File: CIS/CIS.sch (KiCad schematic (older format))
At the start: 181 parts, among them P3 K_0023, U14 U_0101, U16 U_0049, U17 U_0049, U2 STM32H745IIKx

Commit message: Schematic part finished
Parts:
- removed C?: C_0003, DVB_Capacitors_Ceramic:C_0603, symbol CIS-rescue:C_0003-HM3-rescue
- removed C?: C_0007, DVB_Capacitors_Ceramic:C_1206, symbol DVB_C:C_0007
- removed C?: C_0002, DVB_Capacitors_Ceramic:C_0402, symbol CIS-rescue:C_0002-HM3-rescue
- removed F?: F_0002, DVB_F:F_1206, symbol DVB_F:F_0002
- removed K?: K_0042, DVB_Connectors:USB_Mini-B_Lumberg_2486_01_Horizontal, symbol DVB_K:K_0042
- removed L?: L_0009, DVB_Inductors:L_4018-Coilcraft, symbol DVB_L:L_0009
- removed R?: R_0117, DVB_Resistors:R_0402, symbol DVB_R:R_0117
- removed R?: R_0064, DVB_Resistors:R_0402, symbol DVB_R:R_0064
- removed U?: U_0063, DVB_SSOP:MSOP_10-3x3_P0.5, symbol DVB_U:U_0063
- removed U?: U_0054, DVB_SOT:SOT_363-SC_70-6, symbol DVB_U:U_0054
- added C87, C?: C_0002, DVB_Capacitors_Ceramic:C_0402, symbol CIS-rescue:C_0002-HM3-rescue
- added C?: C_0056, DVB_Capacitors_Ceramic:C_0805, symbol DVB_C:C_0056
- added C?: C_0001, DVB_Capacitors_Ceramic:C_0402, symbol DVB_C:C_0001
- added C?: C_0007, DVB_Capacitors_Ceramic:C_1206, symbol DVB_C:C_0007
- added C?: C_0040, DVB_Capacitors_Ceramic:C_1210, symbol DVB_C:C_0040
- added J?: Conn_02x03_Counter_Clockwise, symbol Connector_Generic:Conn_02x03_Counter_Clockwise
- added L?: L_0002, DVB_Inductors:L_5030-Coilcraft, symbol DVB_L:L_0002
- added R?: R_0030, DVB_Resistors:R_0402, symbol DVB_R:R_0030
- added U?: U_1001, DVB_SSOP:MSOP_16-1EP_3x4_P0.5, symbol DVB_U:U_0065
- gave numbers to parts that had none: 119
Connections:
- net labels removed: 5V_PG, AGND, SWO, USB_D+, USB_D-
- wire segments 298 -> 300
- no-connect marks 4 -> 90
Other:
- moved on the sheet: C14, C17, C19, C21, C24, C25, C30, C31, C35, C39, C4, C41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

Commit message: Place components and route POWER + ETHERNET
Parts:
- removed C11, C16, C30, C66, C73, C74, C77, C80, C?: C_0007, DVB_Capacitors_Ceramic:C_1206, symbol DVB_C:C_0007
- removed C13, C15, C18, C81, C83, C85, C?: C_0056, DVB_Capacitors_Ceramic:C_0805, symbol DVB_C:C_0056
- removed C41: C_0037, DVB_Capacitors_Ceramic:C_0603, symbol CIS-rescue:C_0037-HM3-rescue
- removed C50, C51: C_0040, DVB_Capacitors_Ceramic:C_1210, symbol DVB_C:C_0040
- added C11, C16, C30, C7: C_0036, DVB_Capacitors_Ceramic:C_0603, symbol DVB_C:C_0036
- added C13, C15, C18, C41, C81, C83, C85, C88: C_0044, DVB_Capacitors_Ceramic:C_0402, symbol DVB_C:C_0044
- added C66, C73, C74, C77, C80: C_0063, DVB_Capacitors_Ceramic:C_0402, symbol DVB_C:C_0063
- added C91: C_0002, DVB_Capacitors_Ceramic:C_0402, symbol CIS-rescue:C_0002-HM3-rescue
- added C92: C_0053, DVB_Capacitors_Ceramic:C_0805, symbol DVB_C:C_0053
- J4: renamed from J?; value Conn_02x03_Counter_Clockwise -> DEBUG TAG; footprint (none) -> Connector:Tag-Connect_TC2030-IDC-NL_2x03_P1.27mm_Vertical
- P3: footprint DVB_Connectors:K_SHF-105-01-L-D-RA -> DVB_Connectors:SHF-105-01-L-D-TH
- XO1, XO2: footprint DVB_Clock:XO_7M -> DVB_Clock:7M
- gave numbers to parts that had none: 6
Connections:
- net +12V: now also C11.1, C30.1
- net +15: now also C7.2
- net +3.3V: now also C13.1, C66.1, C77.1, C80.1
- net GND: now also R11.1, C11.2, C13.2, C15.2, C16.2, C18.2, C30.2, C41.2, C66.2, C7.1, C73.2, C74.2, C77.2, C80.2, C81.1, C83.1, C85.1, C88.1, C91.2, C92.2; no longer R11.2
- net VERF+: now also R9.1, C83.2; no longer R9.2
- net VERF-: now also R11.2, C85.2, C91.1, C92.1; no longer R11.1
- net at C39.1, U14.6 (VDDCR): now also C41.1
- net at C72.1, C75.1, C76.1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: now also C73.1, C74.1
- net at K1.3 (VP): now also C18.1
- net at K1.4 (VCOMH): now also C16.1
- net at K1.5 (VLOGIC): now also C15.1
- net at C82.1, L7.2, U2.M4 (VDDA): now also C81.2
- net at R6.1, U5.3 (ADJ): now also R9.2; no longer R9.1
- net at U4.13 (INTVcc): now also C88.2
- no-connect marks 90 -> 89
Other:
- moved on the sheet: C14, C25, C52, R10, R11, R6, R9

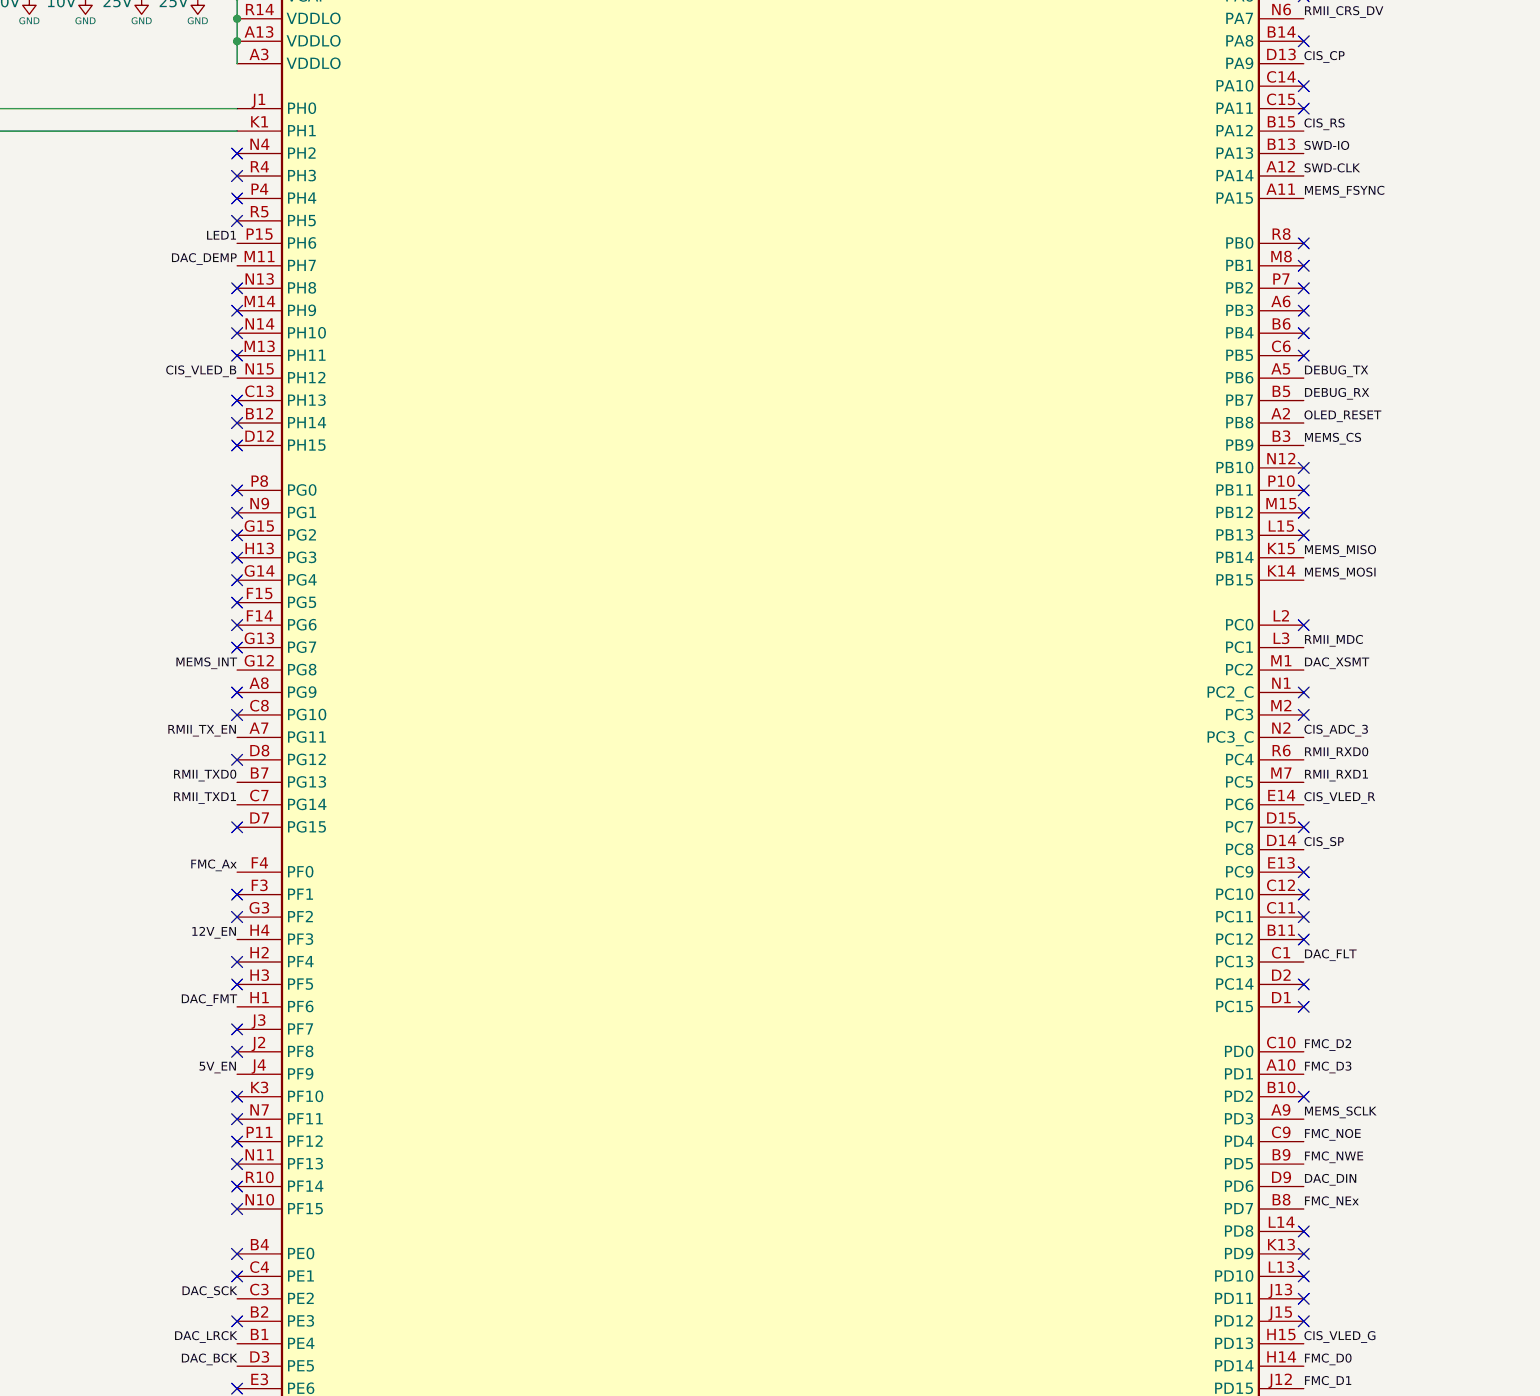
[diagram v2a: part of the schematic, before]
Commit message: First autoroute succes
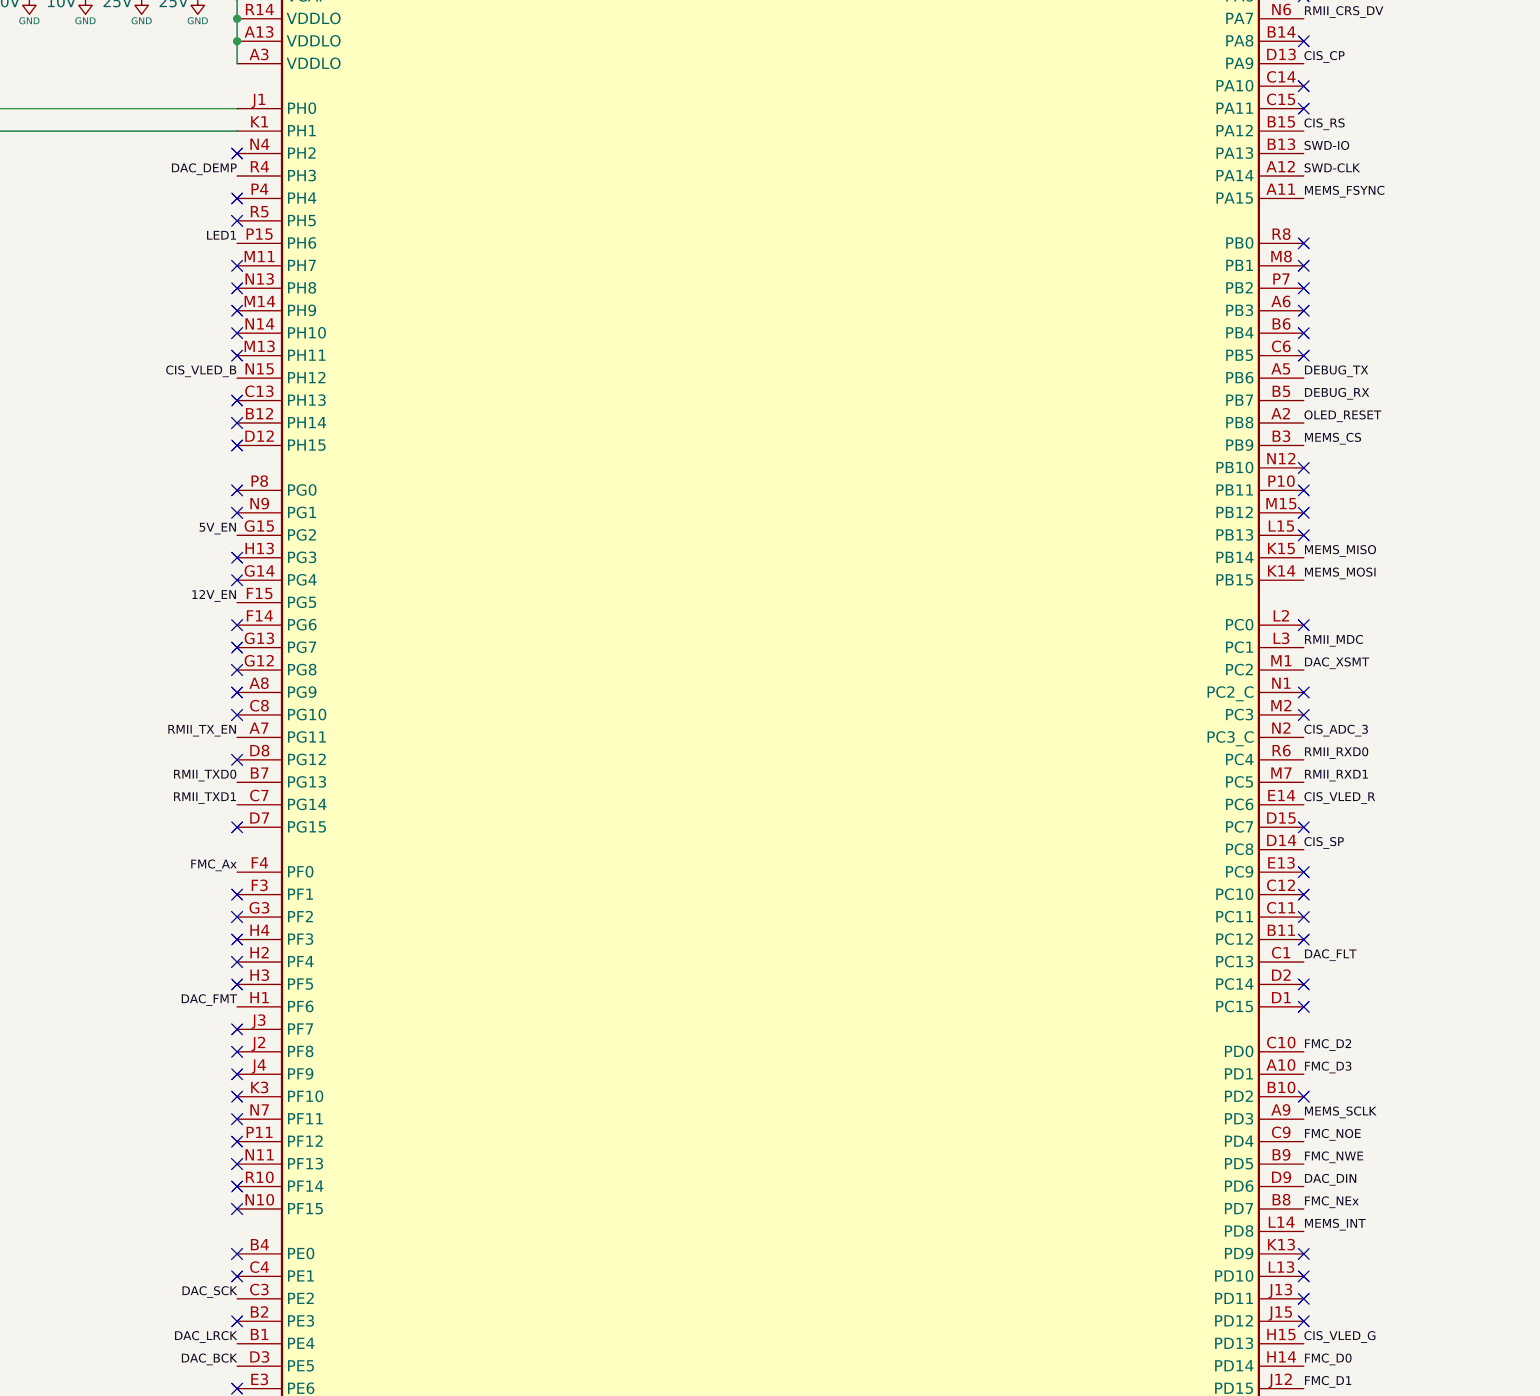
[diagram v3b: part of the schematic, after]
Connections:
- net 12V_EN: now also U2.F15 (PG5); no longer U2.H4 (PF3)
- net 5V_EN: now also U2.G15 (PG2); no longer U2.J4 (PF9)
- net DAC_DEMP: now also U2.R4 (PH3); no longer U2.M11 (PH7)
- net MEMS_INT: now also U2.L14 (PD8); no longer U2.G12 (PG8)
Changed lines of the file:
@@
 Text Label 20400 9425 0    39   ~ 0
 FMC_D0
-Text Label 15650 4525 2    39   ~ 0
+Text Label 15650 4125 2    39   ~ 0
 DAC_DEMP
 Text Label 15650 9325 2    39   ~ 0
@@
 Text Label 15650 7825 2    39   ~ 0
 DAC_FMT
-Text Label 15650 8125 2    39   ~ 0
+Text Label 15650 5725 2    39   ~ 0
 5V_EN
-Text Label 15650 7525 2    39   ~ 0
+Text Label 15650 6025 2    39   ~ 0
 12V_EN
 Text Label 15650 10325 2    39   ~ 0
@@
 Text Label 20400 5325 0    39   ~ 0
 MEMS_CS
-Text Label 15650 6325 2    39   ~ 0
+Text Label 20400 8825 0    39   ~ 0
 MEMS_INT
 Text Label 20400 4225 0    39   ~ 0
@@
 NoConn ~ 20400 7825
 NoConn ~ 20400 8225
-NoConn ~ 20400 8825
+NoConn ~ 15650 6325
 NoConn ~ 20400 8925
 NoConn ~ 20400 9025
@@
 NoConn ~ 15650 6225
 NoConn ~ 15650 6125
-NoConn ~ 15650 6025
 NoConn ~ 15650 5925
 NoConn ~ 15650 5825
-NoConn ~ 15650 5725
 NoConn ~ 15650 5625
 NoConn ~ 15650 5525
@@
 NoConn ~ 15650 4325
 NoConn ~ 15650 4225
-NoConn ~ 15650 4125
+NoConn ~ 15650 4525
 NoConn ~ 15650 4025
 $Comp
@@
 	1    0    0    -1
 $EndComp
+NoConn ~ 15650 8125
+NoConn ~ 15650 7525
 $EndSCHEMATC

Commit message: Update 3d model
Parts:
- J1: footprint Connector_Molex:Molex_PicoBlade_53048-1210_1x12_P1.25mm_Horizontal -> DVB_Connectors:Molex_PicoBlade_53048-1210_1x12_P1.25mm_Horizontal
- J2: footprint Connector_RJ:RJ45_Abracon_ARJP11A-MA_Horizontal -> DVB_Connectors:RJ45_Abracon_ARJP11A-MA_Horizontal
- J3: footprint Connector_Audio:Jack_3.5mm_CUI_SJ1-3533NG_Horizontal -> DVB_Connectors:Jack_3.5mm_CUI_SJ1-3533NG_Horizontal
- K1: footprint DVB_Displays:OLED256x64-2P1_HOLE -> DVB_Displays:OLED256x64-2P1_HOLE_TE_3-2328724-1‎
- U14: footprint DVB_QFN_DFN:QFN-24-1EP_4x4mm_Pitch0.5mm -> DVB_QFN:QFN-24-1EP_4x4mm_Pitch0.5mm
- U8: footprint Package_LGA:LGA-16_3x3mm_P0.5mm_LayoutBorder3x5y -> DVB_LGA:LGA-16_3x3mm_P0.5mm_LayoutBorder3x5y
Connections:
- net CIS_LED_B: now also U2.N15 (PH12)
- net CIS_LED_G: now also U2.H15 (PD13)
- net CIS_LED_R: now also U2.E14 (PC6)
- net CIS_VLED_B: no longer U2.N15 (PH12)
- net CIS_VLED_G: no longer U2.H15 (PD13)
- net CIS_VLED_R: no longer U2.E14 (PC6)
- net GND: now also J2.15 (SHIELD)
- no-connect marks 89 -> 88
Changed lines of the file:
@@
 F 0 "U14" H 9400 14575 60  0000 C CNN
 F 1 "U_0101" H 9400 14675 60  0001 C CNN
-F 2 "DVB_QFN_DFN:QFN-24-1EP_4x4mm_Pitch0.5mm" H 12320 13945 60  0001 C CNN
+F 2 "DVB_QFN:QFN-24-1EP_4x4mm_Pitch0.5mm" H 12320 13945 60  0001 C CNN
 F 3 "http://ww1.microchip.com/downloads/en/DeviceDoc/8742a.pdf" H 11225 13850 60  0001 L CNN
 F 4 "LAN8742A-CZ-TR" H 8925 12275 60  0000 C CNN "Field4"
@@
 F 0 "J2" H 15075 11375 50  0000 C CNN
 F 1 "RJ45_Abracon_ARJP11A-MASA-B-A-EMU2" H 15075 11475 50  0000 C CNN
-F 2 "Connector_RJ:RJ45_Abracon_ARJP11A-MA_Horizontal" H 15075 14275 50  0001 C CNN
+F 2 "DVB_Connectors:RJ45_Abracon_ARJP11A-MA_Horizontal" H 15075 14275 50  0001 C CNN
 F 3 "https://abracon.com/Magnetics/lan/ARJP11A.PDF" H 14925 12025 50  0001 C CNN
 	1    15075 12875
@@
 Wire Wire Line
 	14050 14175 14075 14175
-NoConn ~ 15775 13975
 $Comp
 L DVB_R:R_0075 R51
@@
 F 0 "J3" H 11625 3725 50  0000 C CNN
 F 1 "SJ1-3533NG" H 11625 3625 50  0000 C CNN
-F 2 "Connector_Audio:Jack_3.5mm_CUI_SJ1-3533NG_Horizontal" H 11625 3375 50  0001 C CNN
+F 2 "DVB_Connectors:Jack_3.5mm_CUI_SJ1-3533NG_Horizontal" H 11625 3375 50  0001 C CNN
 F 3 "~" H 11625 3375 50  0001 C CNN
 	1    11625 3375
@@
 F 0 "K1" H 1975 3975 60  0000 C CNN
 F 1 "K_9999" H 2025 2675 60  0001 C CNN
-F 2 "DVB_Displays:OLED256x64-2P1_HOLE" H 2025 2575 60  0001 C CNN
+F 2 "DVB_Displays:OLED256x64-2P1_HOLE_TE_3-2328724-1‎" H 2025 2575 60  0001 C CNN
 F 3 "https://www.crystalfontz.com/products/document/4336/CFAL25664C0-021M-W-YDatasheet.pdf" H 2025 2475 60  0001 C CNN
 F 4 "3-2328724-1‎" H 1975 4075 50  0000 C CNN "Field4"
@@
 F 0 "J1" H 5275 3150 50  0000 C CNN
 F 1 "Conn_01x12" V 5375 2500 50  0000 C CNN
-F 2 "Connector_Molex:Molex_PicoBlade_53048-1210_1x12_P1.25mm_Horizontal" H 5275 2550 50  0001 C CNN
+F 2 "DVB_Connectors:Molex_PicoBlade_53048-1210_1x12_P1.25mm_Horizontal" H 5275 2550 50  0001 C CNN
 F 3 "~" H 5275 2550 50  0001 C CNN
 	1    5275 2550
@@
 F 0 "U8" H 10625 10550 50  0000 L CNN
 F 1 "ICM-20602" H 11425 10550 50  0000 C CNN
-F 2 "Package_LGA:LGA-16_3x3mm_P0.5mm_LayoutBorder3x5y" H 11025 10350 50  0001 C CNN
+F 2 "DVB_LGA:LGA-16_3x3mm_P0.5mm_LayoutBorder3x5y" H 11025 10350 50  0001 C CNN
 F 3 "http://www.invensense.com/wp-content/uploads/2016/10/DS-000176-ICM-20602-v1.0.pdf" H 11075 11050 50  0001 C CNN
 	1    11025 10100
@@
 Text Label 20400 3925 0    39   ~ 0
 CIS_RS
-Text Label 20400 9325 0    39   ~ 0
-CIS_VLED_G
-Text Label 20400 6925 0    39   ~ 0
-CIS_VLED_R
-Text Label 15650 5025 2    39   ~ 0
-CIS_VLED_B
 Text Label 20400 8425 0    39   ~ 0
 FMC_NOE
@@
 NoConn ~ 15650 8125
 NoConn ~ 15650 7525
+$Comp
+L CIS-rescue:GND-HM3-rescue #PWR0192
+U 1 1 5FE373BB
+P 15775 13975
+F 0 "#PWR0192" H 15775 13815 30  0001 C CNN
+F 1 "GND" H 15775 13865 30  0000 C CNN
+F 2 "" H 15675 13625 50  0001 C CNN
+F 3 "" H 15775 13725 50  0001 C CNN
+	1    15775 13975
+	0    -1   1    0
+$EndComp
+Text Label 20400 6925 0    39   ~ 0
+CIS_LED_R
+Text Label 20400 9325 0    39   ~ 0
+CIS_LED_G
+Text Label 15650 5025 2    39   ~ 0
+CIS_LED_B
 $EndSCHEMATC

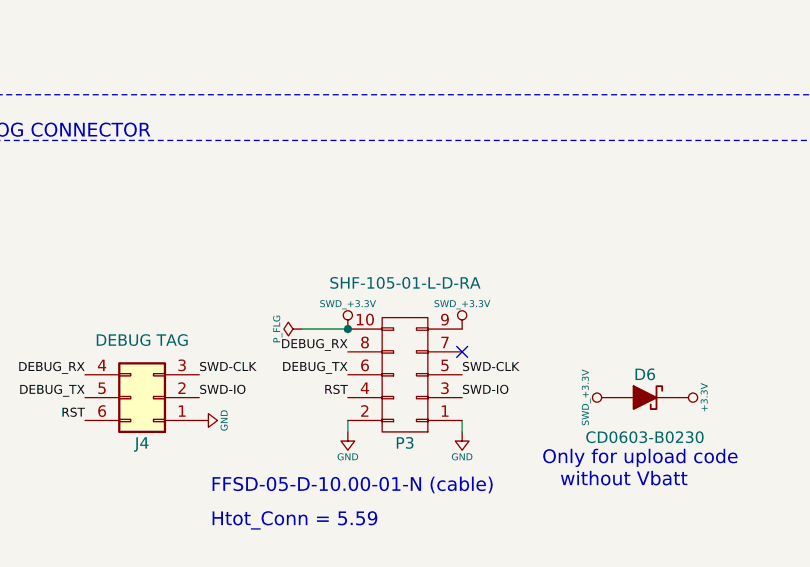
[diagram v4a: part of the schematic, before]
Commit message: Update oled connector / complete 3D missing part
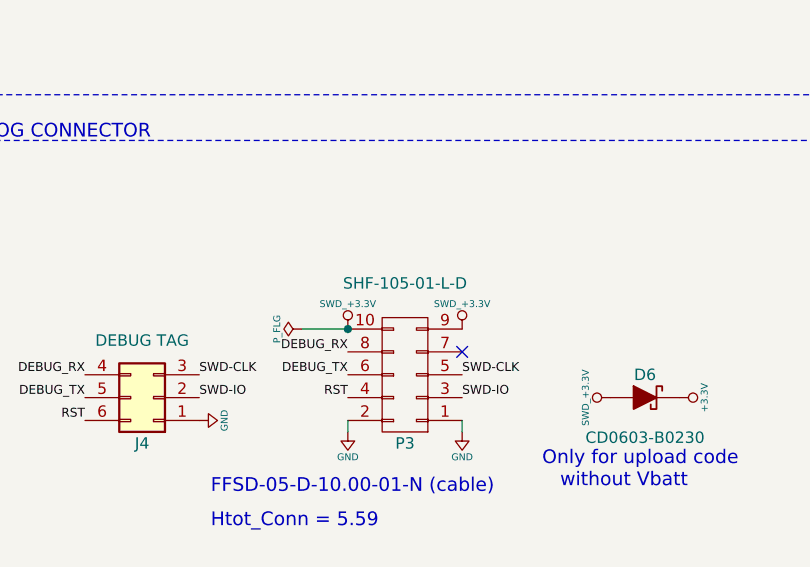
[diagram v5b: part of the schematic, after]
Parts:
- P3: Field1 SHF-105-01-L-D-RA -> SHF-105-01-L-D
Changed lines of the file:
@@
 F 2 "DVB_Connectors:SHF-105-01-L-D-TH" H 10710 6600 50  0001 C CNN
 F 3 "http://www.farnell.com/datasheets/1810787.pdf?_ga=2.121651147.1318262782.1499092899-695518372.1495123464" H 10710 6525 50  0001 C CNN
-F 4 "SHF-105-01-L-D-RA" H 10700 7025 50  0000 C CNN "Field1"
+F 4 "SHF-105-01-L-D" H 10700 7025 50  0000 C CNN "Field1"
 F 5 "SHF-105-01-L-D-RA" H 10710 6750 50  0001 C CNN "Field2"
 F 6 "Samtec" H 10710 6825 50  0001 C CNN "Field3"
